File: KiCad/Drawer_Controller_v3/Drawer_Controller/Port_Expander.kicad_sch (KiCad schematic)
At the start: 1 part, among them U21 PCA9554PW,118

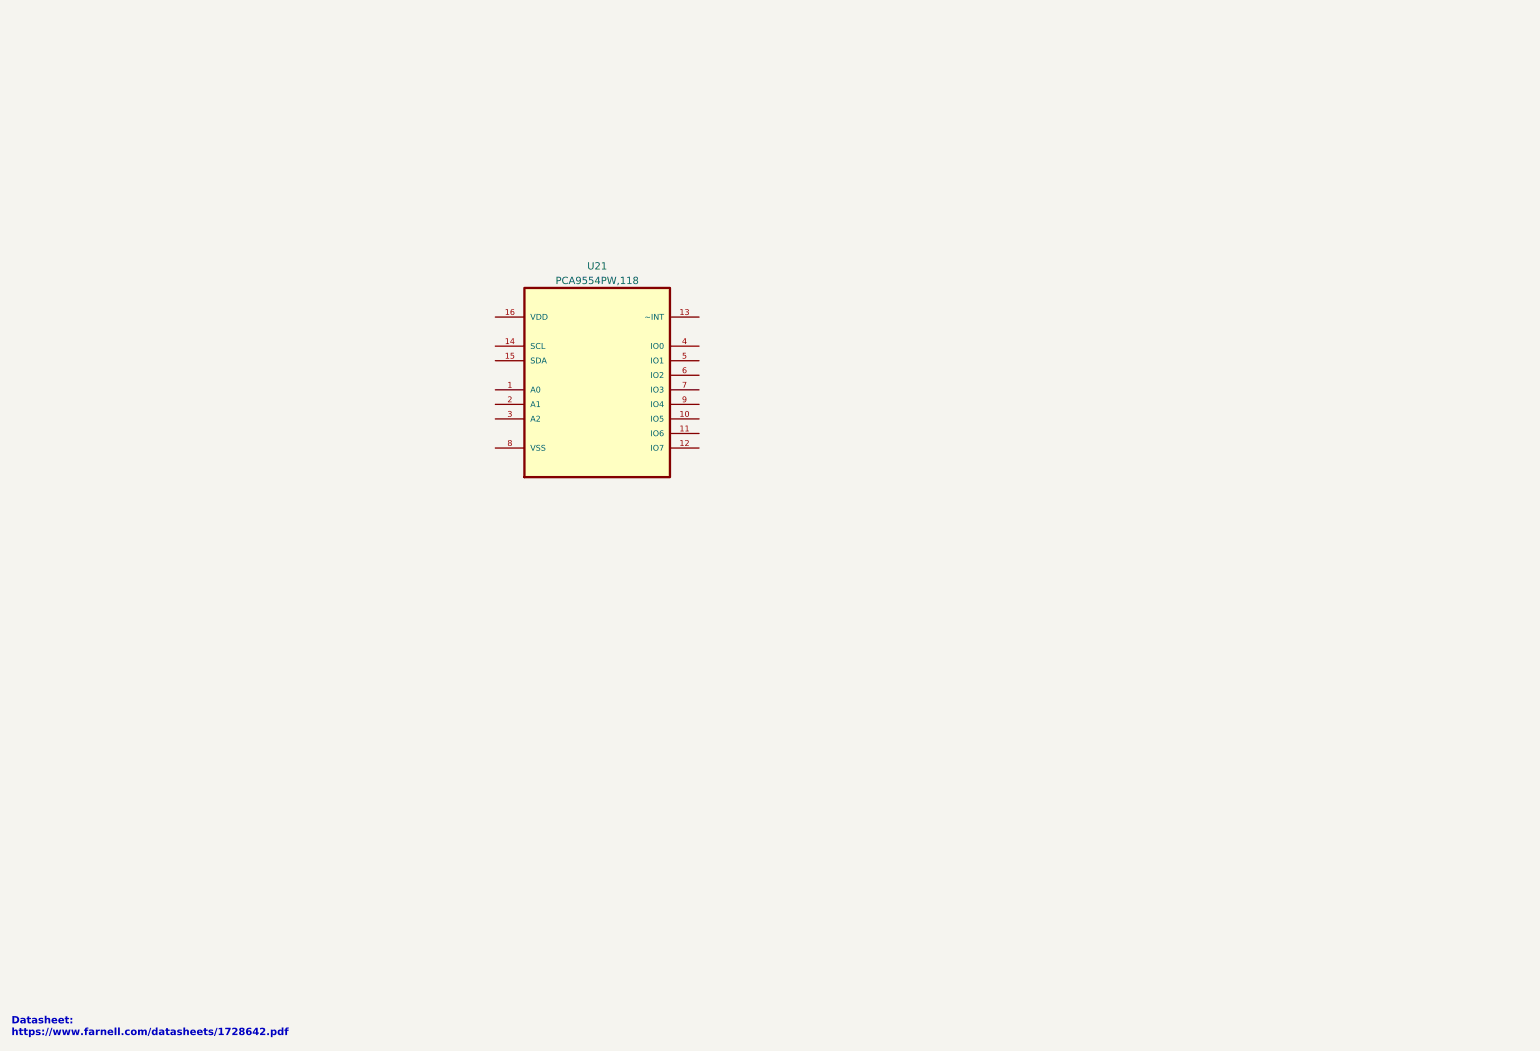
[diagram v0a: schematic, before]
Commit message: Finished adding port expander to schematic
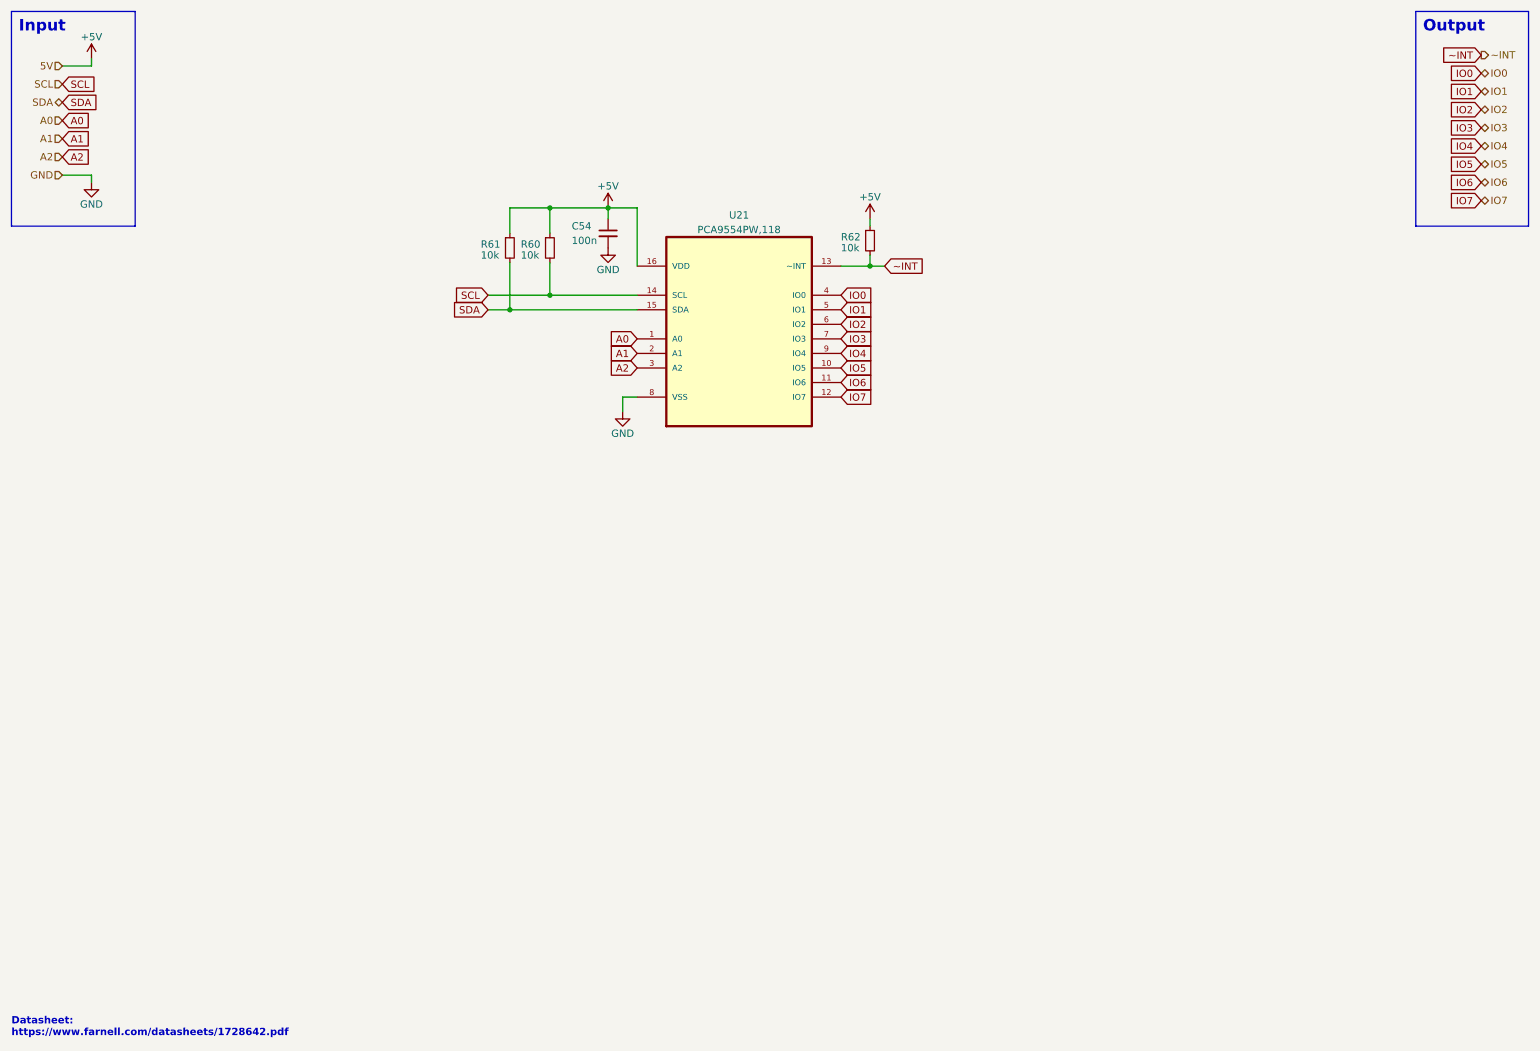
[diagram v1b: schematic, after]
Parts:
- added C54: 100n, symbol Device:C_Small
- added R60, R61, R62: 10k, symbol Device:R_Small
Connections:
- net A0: now reaches U21.1 (A0)
- net IO5: now reaches U21.10 (IO5)
- net IO6: now reaches U21.11 (IO6)
- net IO7: now reaches U21.12 (IO7)
- net ~INT: now reaches U21.13 (~INT)
- net ~INT: now also R62.2
- net SCL: now reaches U21.14 (SCL)
- net SCL: now also R60.2
- net SDA: now reaches U21.15 (SDA)
- net SDA: now also R61.2
- net +5V: now reaches U21.16 (VDD)
- net +5V: now also C54.1, R60.1, R61.1, R62.1
- net A1: now reaches U21.2 (A1)
- net A2: now reaches U21.3 (A2)
- net IO0: now reaches U21.4 (IO0)
- net IO1: now reaches U21.5 (IO1)
- net IO2: now reaches U21.6 (IO2)
- net IO3: now reaches U21.7 (IO3)
- net GND: now reaches U21.8 (VSS)
- net GND: now also C54.2
- net IO4: now reaches U21.9 (IO4)
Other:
- note added: "Input"
- note added: "Output"
- moved on the sheet: U21

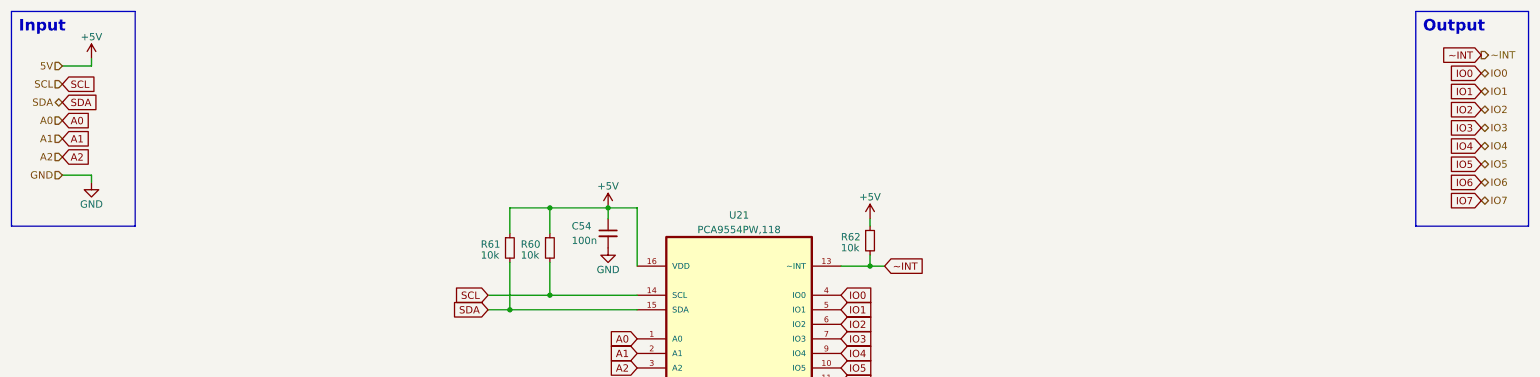
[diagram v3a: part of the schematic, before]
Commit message: Fixing some ERC errors and warnings
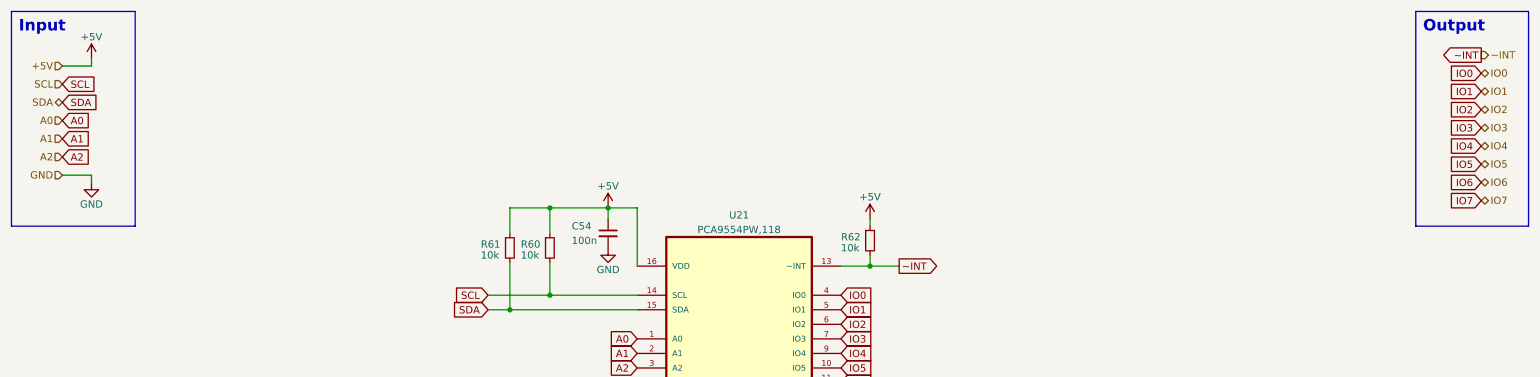
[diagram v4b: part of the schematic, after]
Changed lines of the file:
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@@
     (stroke (width 0) (type default))
   )
-  (wire (pts (xy 168.275 59.69) (xy 165.735 59.69))
+  (wire (pts (xy 170.815 59.69) (xy 165.735 59.69))
     (stroke (width 0) (type default))
   )
@@
     )
   )
-  (global_label "~INT" (shape input) (at 272.415 22.86 180) (fields_autoplaced)
+  (global_label "~INT" (shape output) (at 272.415 22.86 180) (fields_autoplaced)
     (effects (font (size 1.27 1.27)) (justify right))
     (property "Intersheetrefs" "${INTERSHEET_REFS}" (at 265.6992 22.86 0)
@@
     )
   )
-  (global_label "~INT" (shape input) (at 168.275 59.69 0) (fields_autoplaced)
-    (effects (font (size 1.27 1.27)) (justify left))
-    (property "Intersheetrefs" "${INTERSHEET_REFS}" (at 174.9908 59.69 0)
+  (global_label "~INT" (shape output) (at 170.815 59.69 0) (fields_autoplaced)
+    (effects (font (size 1.27 1.27)) (justify left))
+    (property "Intersheetrefs" "${INTERSHEET_REFS}" (at 177.5308 59.69 0)
       (effects (font (size 1.27 1.27)) (justify left) hide)
     )
@@
     (effects (font (size 1.27 1.27)) (justify right))
   )
-  (hierarchical_label "5V" (shape input) (at 24.765 24.765 180) (fields_autoplaced)
-    (effects (font (size 1.27 1.27)) (justify right))
-  )
+  (hierarchical_label "+5V" (shape input) (at 24.765 24.765 180) (fields_autoplaced)
+    (effects (font (size 1.27 1.27)) (justify right))
+  )

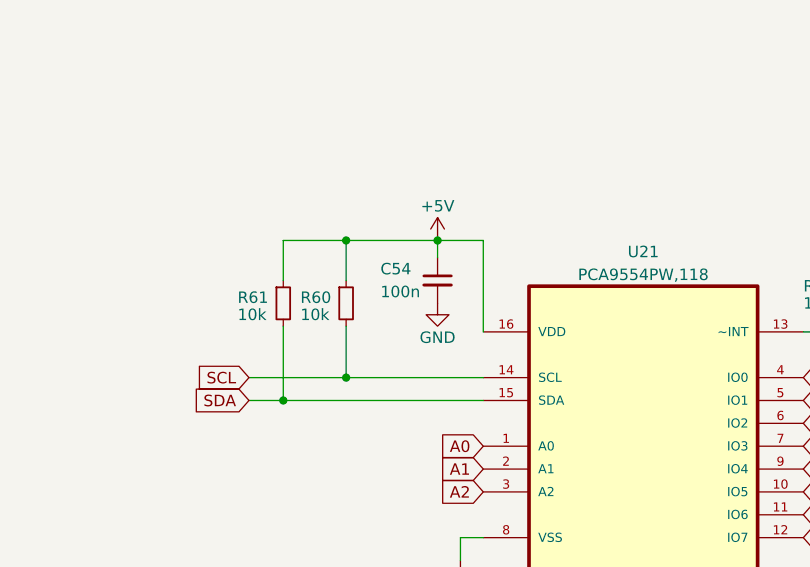
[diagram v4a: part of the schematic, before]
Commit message: Finished assigning all footprints
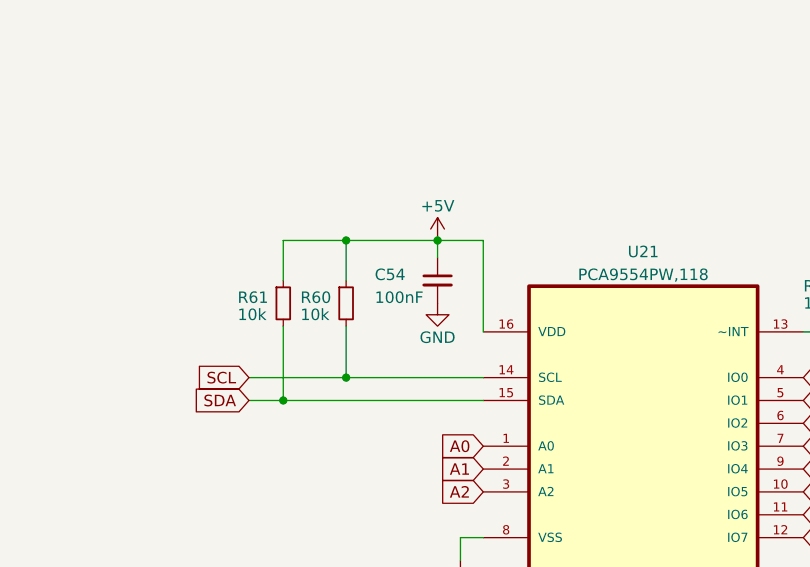
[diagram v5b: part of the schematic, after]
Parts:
- C54: value 100n -> 100nF; footprint (none) -> Capacitor_SMD:C_0402_1005Metric
- R60, R61, R62: footprint (none) -> Capacitor_SMD:C_0603_1608Metric
- U21: footprint SOP65P640X110-16N -> Robast_Footprints:PCA9554PW_118
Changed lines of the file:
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@@
       (effects (font (size 1.27 1.27)) (justify left))
     )
-    (property "Footprint" "" (at 109.855 56.515 0)
+    (property "Footprint" "Capacitor_SMD:C_0603_1608Metric" (at 109.855 56.515 0)
       (effects (font (size 1.27 1.27)) hide)
     )
@@
   (symbol (lib_id "Device:C_Small") (at 120.015 53.975 0) (unit 1)
     (in_bom yes) (on_board yes) (dnp no)
-    (property "Reference" "C54" (at 113.665 52.705 0)
-      (effects (font (size 1.27 1.27)) (justify left))
-    )
-    (property "Value" "100n" (at 113.665 55.245 0)
-      (effects (font (size 1.27 1.27)) (justify left))
-    )
-    (property "Footprint" "" (at 120.015 53.975 0)
+    (property "Reference" "C54" (at 113.03 53.34 0)
+      (effects (font (size 1.27 1.27)) (justify left))
+    )
+    (property "Value" "100nF" (at 113.03 55.88 0)
+      (effects (font (size 1.27 1.27)) (justify left))
+    )
+    (property "Footprint" "Capacitor_SMD:C_0402_1005Metric" (at 120.015 53.975 0)
       (effects (font (size 1.27 1.27)) hide)
     )
@@
       (effects (font (size 1.27 1.27)))
     )
-    (property "Footprint" "SOP65P640X110-16N" (at 142.875 67.31 0)
+    (property "Footprint" "Robast_Footprints:PCA9554PW_118" (at 142.875 67.31 0)
       (effects (font (size 1.27 1.27)) (justify bottom) hide)
     )
@@
       (effects (font (size 1.27 1.27)) (justify left))
     )
-    (property "Footprint" "" (at 102.87 56.515 0)
+    (property "Footprint" "Capacitor_SMD:C_0603_1608Metric" (at 102.87 56.515 0)
       (effects (font (size 1.27 1.27)) hide)
     )
@@
       (effects (font (size 1.27 1.27)) (justify left))
     )
-    (property "Footprint" "" (at 165.735 55.245 0)
-      (effects (font (size 1.27 1.27)) hide)
-    )
+    (property "Footprint" "Capacitor_SMD:C_0603_1608Metric" (at 165.735 55.245 0)
+      (effects (font (size 1.27 1.27)) hide)
+    )

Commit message: Starting routing the PCB - WIP
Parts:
- removed R60, R61: 10k, Capacitor_SMD:C_0603_1608Metric, symbol Device:R_Small
- R62: footprint Capacitor_SMD:C_0603_1608Metric -> Resistor_SMD:R_0402_1005Metric
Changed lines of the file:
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@@
   (junction (at 165.735 59.69) (diameter 0) (color 0 0 0 0)
   )
-  (junction (at 109.855 64.77) (diameter 0) (color 0 0 0 0)
-  )
-  (junction (at 109.855 49.53) (diameter 0) (color 0 0 0 0)
-  )
-  (junction (at 102.87 67.31) (diameter 0) (color 0 0 0 0)
-  )
   (wire (pts (xy 29.845 43.815) (xy 29.845 45.085))
     (stroke (width 0) (type default))
   )
-  (wire (pts (xy 102.87 49.53) (xy 109.855 49.53))
-    (stroke (width 0) (type default))
-  )
-  (wire (pts (xy 99.06 64.77) (xy 109.855 64.77))
-    (stroke (width 0) (type default))
-  )
   (wire (pts (xy 24.765 43.815) (xy 29.845 43.815))
     (stroke (width 0) (type default))
   )
-  (wire (pts (xy 99.06 67.31) (xy 102.87 67.31))
-    (stroke (width 0) (type default))
-  )
   (wire (pts (xy 122.555 85.09) (xy 122.555 82.55))
     (stroke (width 0) (type default))
@@
     (stroke (width 0) (type default))
   )
-  (wire (pts (xy 109.855 53.975) (xy 109.855 49.53))
-    (stroke (width 0) (type default))
-  )
-  (wire (pts (xy 109.855 59.055) (xy 109.855 64.77))
-    (stroke (width 0) (type default))
-  )
   (wire (pts (xy 125.095 59.69) (xy 125.095 49.53))
     (stroke (width 0) (type default))
   )
-  (wire (pts (xy 102.87 53.975) (xy 102.87 49.53))
-    (stroke (width 0) (type default))
-  )
   (wire (pts (xy 122.555 82.55) (xy 125.095 82.55))
     (stroke (width 0) (type default))
@@
     (stroke (width 0) (type default))
   )
-  (wire (pts (xy 102.87 59.055) (xy 102.87 67.31))
-    (stroke (width 0) (type default))
-  )
   (wire (pts (xy 165.735 51.435) (xy 165.735 52.705))
     (stroke (width 0) (type default))
@@
     (stroke (width 0) (type default))
   )
-  (wire (pts (xy 109.855 64.77) (xy 125.095 64.77))
+  (wire (pts (xy 99.06 64.77) (xy 125.095 64.77))
     (stroke (width 0) (type default))
   )
@@
     (stroke (width 0) (type default))
   )
-  (wire (pts (xy 109.855 49.53) (xy 120.015 49.53))
-    (stroke (width 0) (type default))
-  )
-  (wire (pts (xy 102.87 67.31) (xy 125.095 67.31))
+  (wire (pts (xy 99.06 67.31) (xy 125.095 67.31))
     (stroke (width 0) (type default))
   )
@@
     (effects (font (size 1.27 1.27)) (justify left))
   )
-  (symbol (lib_id "Device:R_Small") (at 109.855 56.515 0) (unit 1)
-    (in_bom yes) (on_board yes) (dnp no)
-    (property "Reference" "R60" (at 104.775 55.88 0)
-      (effects (font (size 1.27 1.27)) (justify left))
-    )
-    (property "Value" "10k" (at 104.775 57.785 0)
-      (effects (font (size 1.27 1.27)) (justify left))
-    )
-    (property "Footprint" "Capacitor_SMD:C_0603_1608Metric" (at 109.855 56.515 0)
-      (effects (font (size 1.27 1.27)) hide)
-    )
-    (property "Datasheet" "~" (at 109.855 56.515 0)
-      (effects (font (size 1.27 1.27)) hide)
-    )
-    (pin "1")
-    (pin "2")
-    (instances
-      (project "Drawer_Controller"
-        (path "/9538e4ed-27e6-4c37-b989-9859dc0d49e8/83c4ae5d-d64f-40dd-979e-e38a8ced97c0/18a76fdc-0e09-49e0-9380-806c2f315ad0"
-          (reference "R60") (unit 1)
-        )
-        (path "/9538e4ed-27e6-4c37-b989-9859dc0d49e8/83c4ae5d-d64f-40dd-979e-e38a8ced97c0/1fcbb1e1-6aeb-48e2-9242-5118d9fed048"
-          (reference "R67") (unit 1)
-        )
-        (path "/9538e4ed-27e6-4c37-b989-9859dc0d49e8/83c4ae5d-d64f-40dd-979e-e38a8ced97c0/f03c438d-6557-40e8-86f2-af45e49f73d5"
-          (reference "R69") (unit 1)
-        )
-      )
-    )
-  )
   (symbol (lib_id "Device:C_Small") (at 120.015 53.975 0) (unit 1)
     (in_bom yes) (on_board yes) (dnp no)
     (property "Reference" "C54" (at 113.03 53.34 0)
-      (effects (font (size 1.27 1.27)) (justify left))
+      (effects (font (size 1.27 1.27)) (justify left) hide)
     )
     (property "Value" "100nF" (at 113.03 55.88 0)
-      (effects (font (size 1.27 1.27)) (justify left))
+      (effects (font (size 1.27 1.27)) (justify left) hide)
     )
     (property "Footprint" "Capacitor_SMD:C_0402_1005Metric" (at 120.015 53.975 0)
@@
     )
   )
-  (symbol (lib_id "Device:R_Small") (at 102.87 56.515 0) (unit 1)
-    (in_bom yes) (on_board yes) (dnp no)
-    (property "Reference" "R61" (at 97.79 55.88 0)
-      (effects (font (size 1.27 1.27)) (justify left))
-    )
-    (property "Value" "10k" (at 97.79 57.785 0)
-      (effects (font (size 1.27 1.27)) (justify left))
-    )
-    (property "Footprint" "Capacitor_SMD:C_0603_1608Metric" (at 102.87 56.515 0)
-      (effects (font (size 1.27 1.27)) hide)
-    )
-    (property "Datasheet" "~" (at 102.87 56.515 0)
-      (effects (font (size 1.27 1.27)) hide)
-    )
-    (pin "1")
-    (pin "2")
-    (instances
-      (project "Drawer_Controller"
-        (path "/9538e4ed-27e6-4c37-b989-9859dc0d49e8/83c4ae5d-d64f-40dd-979e-e38a8ced97c0/18a76fdc-0e09-49e0-9380-806c2f315ad0"
-          (reference "R61") (unit 1)
-        )
-        (path "/9538e4ed-27e6-4c37-b989-9859dc0d49e8/83c4ae5d-d64f-40dd-979e-e38a8ced97c0/1fcbb1e1-6aeb-48e2-9242-5118d9fed048"
-          (reference "R66") (unit 1)
-        )
-        (path "/9538e4ed-27e6-4c37-b989-9859dc0d49e8/83c4ae5d-d64f-40dd-979e-e38a8ced97c0/f03c438d-6557-40e8-86f2-af45e49f73d5"
-          (reference "R63") (unit 1)
-        )
-      )
-    )
-  )
   (symbol (lib_id "power:GND") (at 120.015 56.515 0) (unit 1)
     (in_bom yes) (on_board yes) (dnp no)
@@
       (effects (font (size 1.27 1.27)) (justify left))
     )
-    (property "Footprint" "Capacitor_SMD:C_0603_1608Metric" (at 165.735 55.245 0)
-      (effects (font (size 1.27 1.27)) hide)
-    )
+    (property "Footprint" "Resistor_SMD:R_0402_1005Metric" (at 165.735 55.245 0)
+      (effects (font (size 1.27 1.27)) hide)
+    )

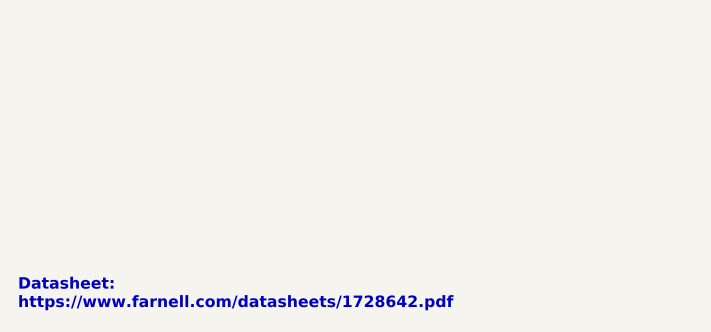
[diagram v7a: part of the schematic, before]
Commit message: Added another link to datasheet of pca9554 port expander
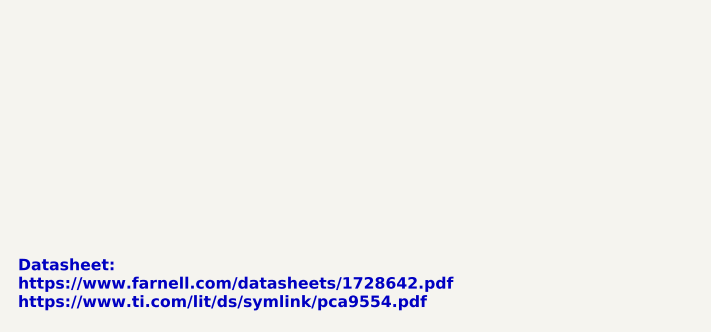
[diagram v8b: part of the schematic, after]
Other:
- note added: "Datasheet: https://www.farnell.com/datasheets/1728642.pdf https://www.ti.com/lit/ds/symlink/pca9554.pdf"
- note removed: "Datasheet: https://www.farnell.com/datasheets/1728642.pdf"
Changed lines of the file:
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@@
     (effects (font (size 2 2) (thickness 0.4) bold) (justify left bottom))
   )
-  (text "Datasheet:\nhttps://www.farnell.com/datasheets/1728642.pdf"
+  (text "Datasheet:\nhttps://www.farnell.com/datasheets/1728642.pdf\nhttps://www.ti.com/lit/ds/symlink/pca9554.pdf"
     (at 15.875 194.31 0)
     (effects (font (size 1.27 1.27) bold) (justify left bottom))
